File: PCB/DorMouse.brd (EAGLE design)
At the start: 40.9 x 69.4 mm, 59 parts, among them IC1 LM340MP-05, IC2 MAX1551, U1 STM32F10XRXT6, X1 MINI-USB-UX60-MB-5ST

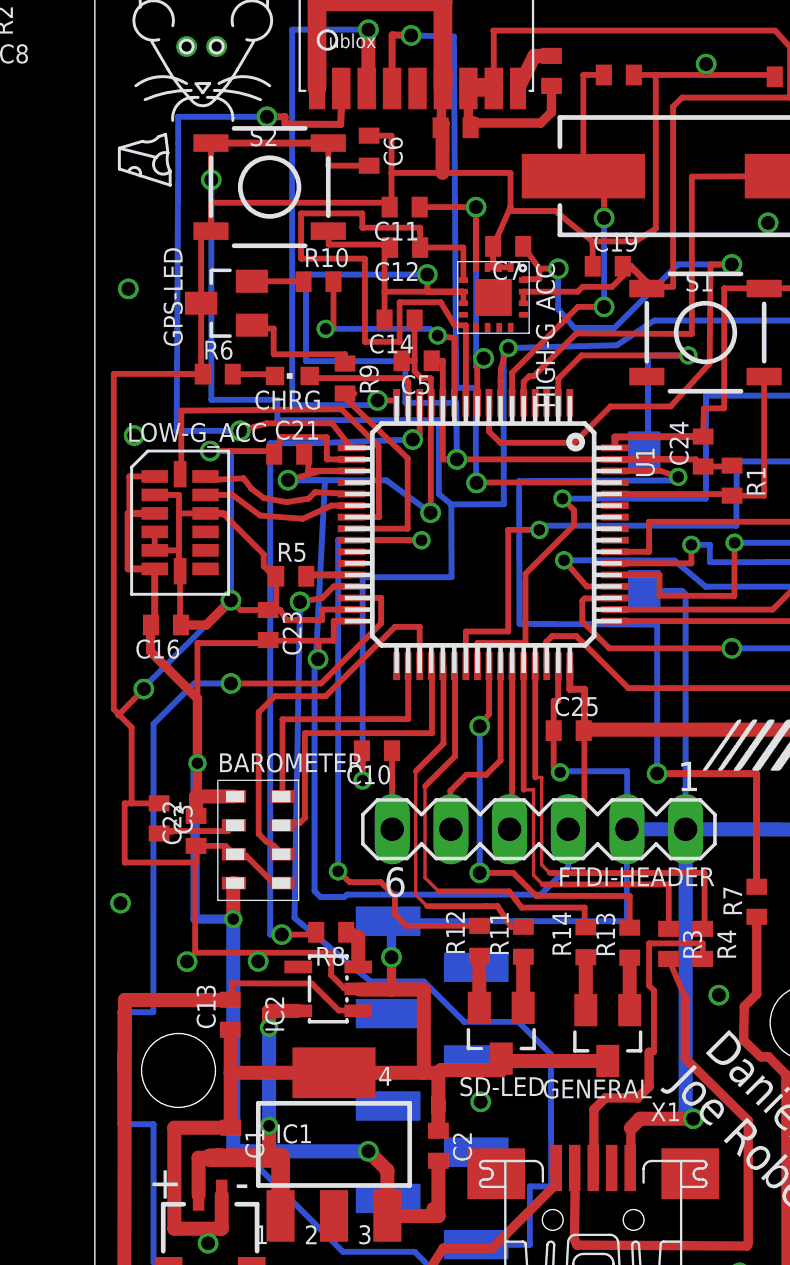
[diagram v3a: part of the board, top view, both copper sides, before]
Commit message: Add labels for GPS
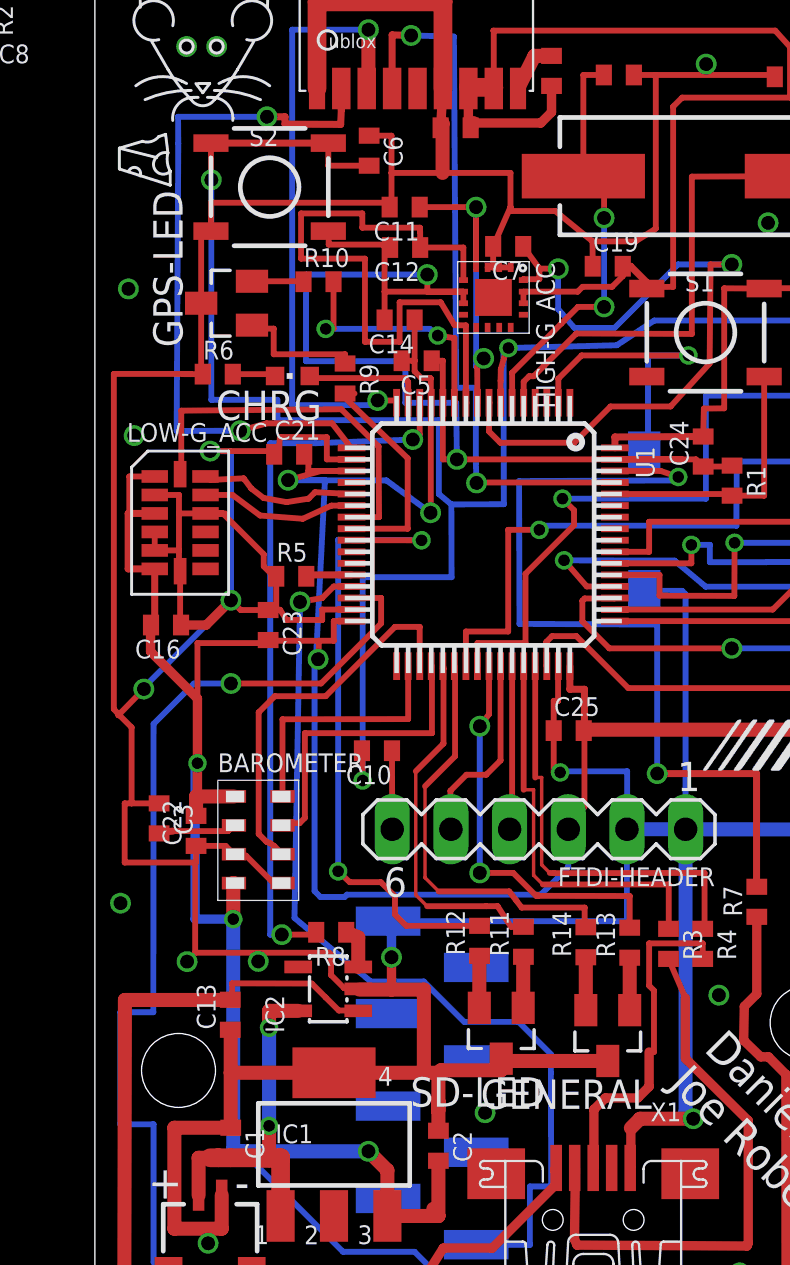
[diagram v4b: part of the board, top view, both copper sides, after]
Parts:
- CHRG: value (none) -> CHRG
- GENERAL: value RED-GREEN_LED -> Status
- GPS-LED: value RED-GREEN_LED -> GPS
- SD-LED: value RED-GREEN_LED -> SD-C
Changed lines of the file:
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@@
 <layer number="20" name="Dimension" color="15" fill="1" visible="yes" active="yes"/>
 <layer number="21" name="tPlace" color="7" fill="1" visible="yes" active="yes"/>
-<layer number="22" name="bPlace" color="7" fill="1" visible="yes" active="yes"/>
+<layer number="22" name="bPlace" color="7" fill="1" visible="no" active="yes"/>
 <layer number="23" name="tOrigins" color="15" fill="1" visible="yes" active="yes"/>
 <layer number="24" name="bOrigins" color="15" fill="1" visible="no" active="yes"/>
@@
 <element name="C2" library="rcl" package="C0402" value="0.1uF" x="14.87" y="9.63" smashed="yes" rot="R270">
 <attribute name="NAME" x="15.505" y="10.265" size="0.8128" layer="25" font="vector" rot="R270"/>
-<attribute name="VALUE" x="15.705" y="9.915" size="0.8128" layer="27" font="vector"/>
+<attribute name="VALUE" x="15.505" y="9.585" size="0.8128" layer="27" font="vector"/>
 </element>
 <element name="IC2" library="maxim" package="SOT23-5L" value="MAX1551" x="10.1" y="16.42" smashed="yes" rot="R90">
@@
 <attribute name="VALUE" x="6.675" y="49.094" size="0.4064" layer="27"/>
 </element>
-<element name="GPS-LED" library="DorMouse" package="SOT23" value="RED-GREEN_LED" x="5.7" y="46.1" smashed="yes" rot="R90">
-<attribute name="NAME" x="3.795" y="44.195" size="0.8128" layer="25" font="vector" rot="R90"/>
-</element>
-<element name="SD-LED" library="DorMouse" package="SOT23" value="RED-GREEN_LED" x="17.59" y="14.5" smashed="yes" rot="R180">
-<attribute name="NAME" x="19.495" y="12.595" size="0.8128" layer="25" font="vector" rot="R180"/>
-</element>
-<element name="GENERAL" library="DorMouse" package="SOT23" value="RED-GREEN_LED" x="22.2" y="14.4" smashed="yes" rot="R180">
-<attribute name="NAME" x="24.105" y="12.495" size="0.8128" layer="25" font="vector" rot="R180"/>
+<element name="GPS-LED" library="DorMouse" package="SOT23" value="GPS" x="5.7" y="46.1" smashed="yes" rot="R90">
+<attribute name="NAME" x="3.795" y="44.195" size="1.27" layer="25" rot="R90"/>
+<attribute name="VALUE" x="3.455" y="44.995" size="1.016" layer="27" font="vector" rot="R90"/>
+</element>
+<element name="SD-LED" library="DorMouse" package="SOT23" value="SD-C" x="17.59" y="14.5" smashed="yes" rot="R180">
+<attribute name="NAME" x="19.495" y="12.595" size="1.27" layer="25" rot="R180"/>
+<attribute name="VALUE" x="16.055" y="11.925" size="0.8128" layer="27" font="vector"/>
+</element>
+<element name="GENERAL" library="DorMouse" package="SOT23" value="Status" x="22.2" y="14.4" smashed="yes" rot="R180">
+<attribute name="NAME" x="24.105" y="12.495" size="1.27" layer="25" rot="R180"/>
+<attribute name="VALUE" x="20.425" y="11.975" size="0.8128" layer="27" font="vector"/>
 </element>
 <element name="R9" library="rcl" package="R0402" value="160" x="10.83" y="42.84" smashed="yes" rot="R270">
@@
 <attribute name="VALUE" x="12.455" y="49.095" size="0.6096" layer="27" font="vector"/>
 </element>
-<element name="CHRG" library="led" package="CHIPLED_0603" value="" x="8.55" y="42.95" smashed="yes" rot="R90">
-<attribute name="NAME" x="9.82" y="42.315" size="0.8128" layer="25" font="vector" rot="R180"/>
-<attribute name="VALUE" x="9.82" y="44.855" size="1.27" layer="27" rot="R180"/>
+<element name="CHRG" library="led" package="CHIPLED_0603" value="CHRG" x="8.55" y="42.95" smashed="yes" rot="R90">
+<attribute name="NAME" x="9.82" y="42.315" size="1.27" layer="25" rot="R180"/>
+<attribute name="VALUE" x="7.16" y="41.495" size="0.8128" layer="27" font="vector"/>
 </element>
 <element name="R6" library="rcl" package="R0402" value="160" x="5.32" y="43.03" smashed="yes">
@@
 <via x="11.18" y="1.37" extent="1-16" drill="0.6"/>
 <via x="27.91" y="4.13" extent="1-16" drill="0.6"/>
-<via x="16.7" y="11.53" extent="1-16" drill="0.6"/>
+<via x="16.89" y="11.06" extent="1-16" drill="0.6"/>
 <via x="27.01" y="16.15" extent="1-16" drill="0.6" shape="octagon"/>
 <via x="31.39" y="18.28" extent="1-16" drill="0.6" shape="octagon"/>

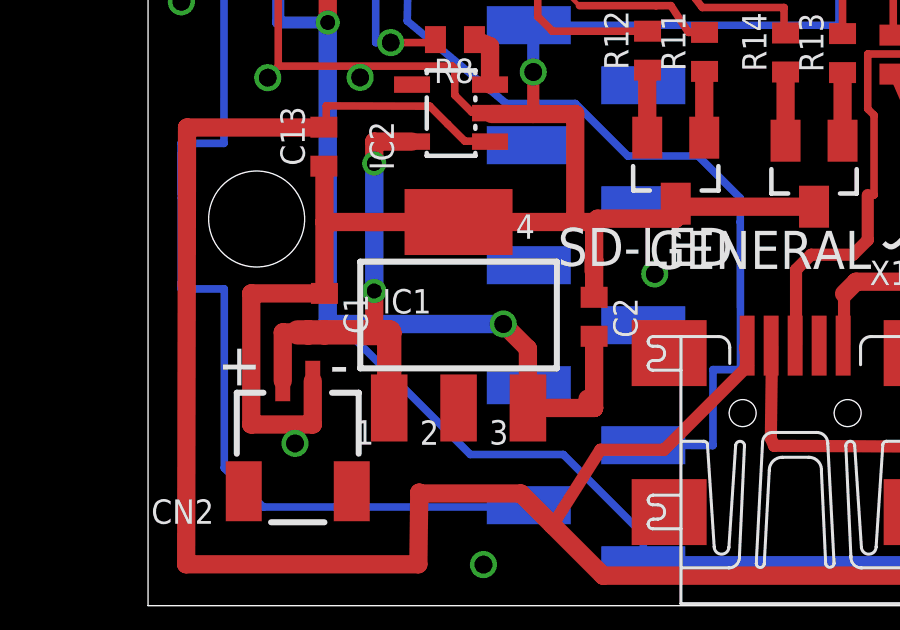
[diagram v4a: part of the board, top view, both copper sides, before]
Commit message: Connect pad 2 of LDO reg to GND
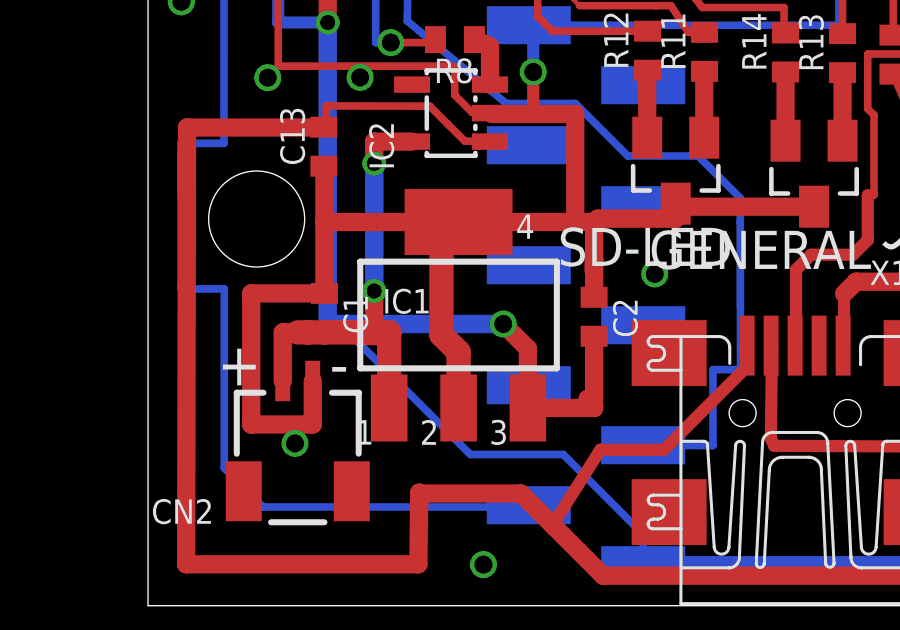
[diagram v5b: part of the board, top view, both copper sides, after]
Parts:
- IC1: device linear:SOT223 -> DorMouse:SOT223
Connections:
- net GND: now also IC1.2
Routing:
- net GND: track 386.2 -> 392.9 mm
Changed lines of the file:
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@@
 <attribute name="VALUE" x="27.153" y="40.49" size="0.4064" layer="28" ratio="10" rot="MR270"/>
 </element>
-<element name="IC1" library="linear" package="SOT223" value="LM340MP-05" x="10.35" y="9.69" smashed="yes">
+<element name="IC1" library="DorMouse" package="SOT223" value="LM340MP-05" x="10.35" y="9.69" smashed="yes">
 <attribute name="NAME" x="7.81" y="9.7408" size="0.8128" layer="25" font="vector"/>
 </element>
@@
 <via x="3.97" y="57.21" extent="1-16" drill="0.6"/>
 <via x="5.27" y="57.21" extent="1-16" drill="0.6"/>
+<contactref element="IC1" pad="2"/>
+<wire x1="10.35" y1="6.5912" x2="10.35" y2="8.46" width="0.8128" layer="1"/>
+<wire x1="10.35" y1="8.46" x2="9.78" y2="9.03" width="0.8128" layer="1"/>
+<wire x1="9.78" y1="9.03" x2="9.78" y2="12.219" width="0.8128" layer="1"/>
+<wire x1="9.78" y1="12.219" x2="10.35" y2="12.789" width="0.8128" layer="1"/>
 </signal>
 <signal name="VCC">
